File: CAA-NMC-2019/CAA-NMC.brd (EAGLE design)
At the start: 33.3 x 100 mm, 28 parts, among them IC1 ATTINY85-20SU, J1 M20-9980346

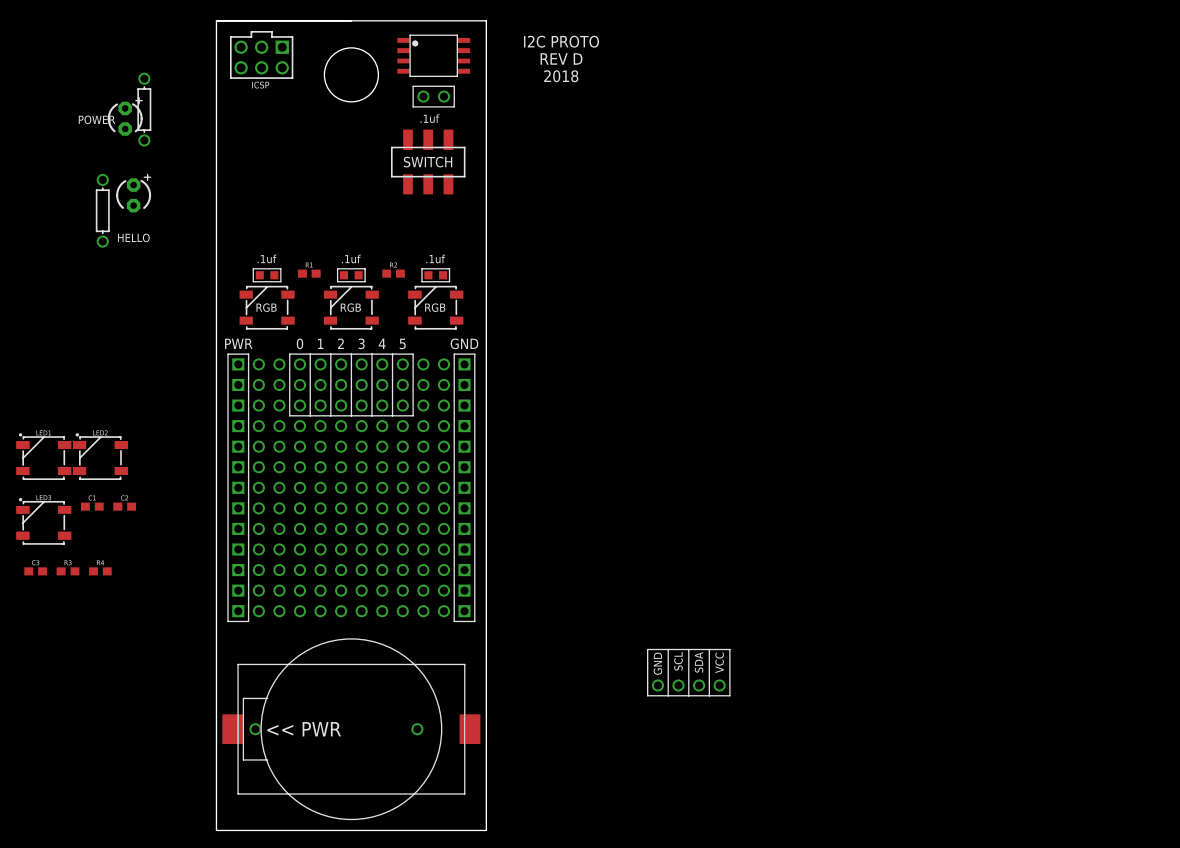
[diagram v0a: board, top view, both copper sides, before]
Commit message: four panel pcb design with snap apart tabs v1
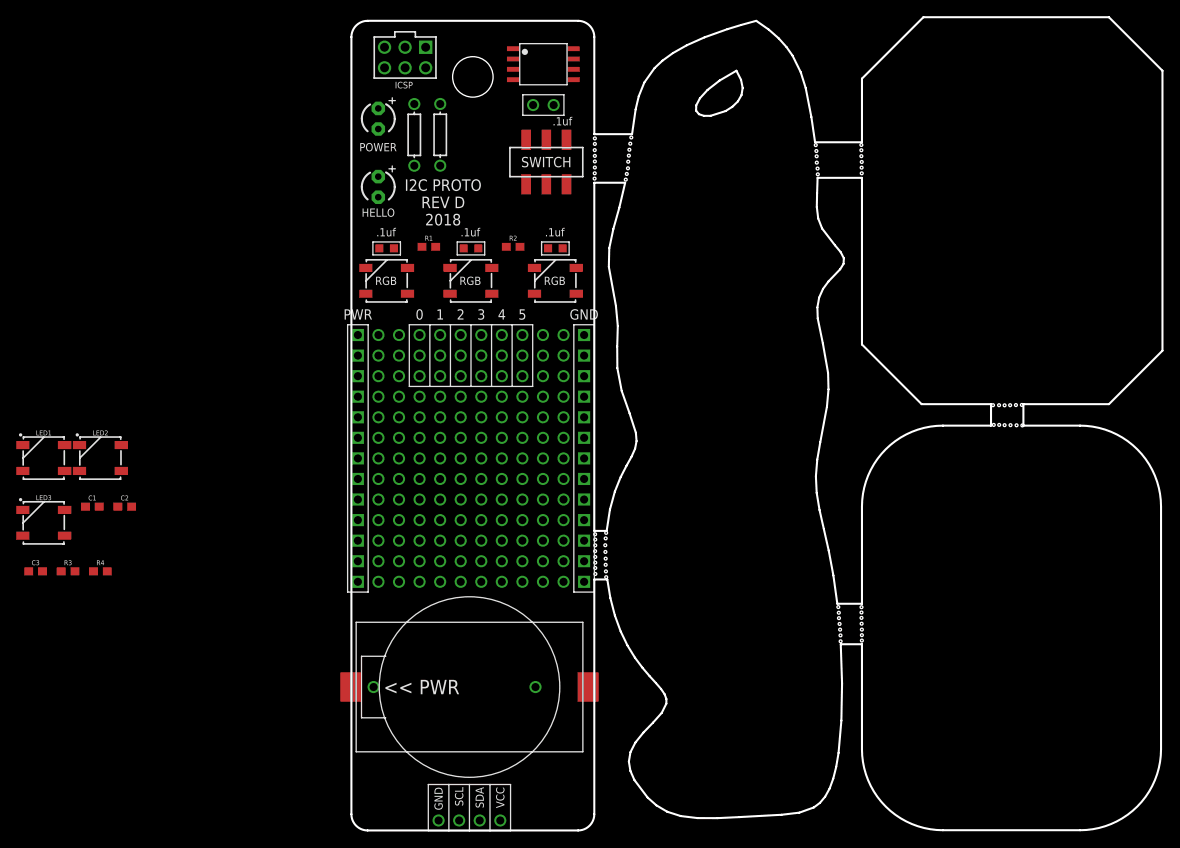
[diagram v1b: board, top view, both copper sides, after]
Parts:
- moved U$127 42.7 mm to (11.0, 85.9)
- moved U$126 33.5 mm to (7.77, 85.9)
- moved U$71 31.8 mm to (10.8, 1.23)
- moved U$72 31.8 mm to (15.8, 1.23)
- moved U$73 31.8 mm to (13.3, 1.23)
- moved U$74 31.8 mm to (18.4, 1.23)
- moved POWER 31.3 mm to (3.32, 87.9)
- moved HELLO 30.2 mm to (3.32, 79.5)
- moved J1 17.7 mm to (6.63, 92.9)
- moved U$2 15.5 mm to (14.6, 17.7)
- moved U$3 15.5 mm to (14.6, 17.7)
- moved U$1 15.2 mm to (14.8, 30.7)
- moved D3 15.1 mm to (25.2, 67.9)
- moved D1 15.1 mm to (4.36, 67.9)
- moved D2 15.1 mm to (14.8, 67.9)
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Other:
- board size 33.3 x 100 mm -> 100.2 x 100.4 mm

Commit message: Roll back to boring profile
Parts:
- moved U$127 42.7 mm to (-30.7, 76.5)
- moved U$126 33.5 mm to (-25.6, 89.0)
- moved U$71 31.8 mm to (37.9, 17.9)
- moved U$72 31.8 mm to (42.9, 17.9)
- moved U$73 31.8 mm to (40.4, 17.9)
- moved U$74 31.8 mm to (45.5, 17.9)
- moved POWER 31.3 mm to (-27.9, 87.9)
- moved HELLO 30.2 mm to (-26.9, 78.4)
- moved J1 17.7 mm to (-11.1, 92.9)
- moved U$2 15.5 mm to (0.00, 12.5)
- moved U$3 15.5 mm to (0.00, 12.5)
- moved U$1 15.2 mm to (0.00, 27.1)
- moved D3 15.1 mm to (10.4, 64.6)
- moved D1 15.1 mm to (-10.4, 64.6)
- moved D2 15.1 mm to (-0.01, 64.6)
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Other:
- board size 100.2 x 100.4 mm -> 33.3 x 100 mm
